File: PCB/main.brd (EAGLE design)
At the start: 98.1 x 68.5 mm, 81 parts, among them X1 BU-SMA-V

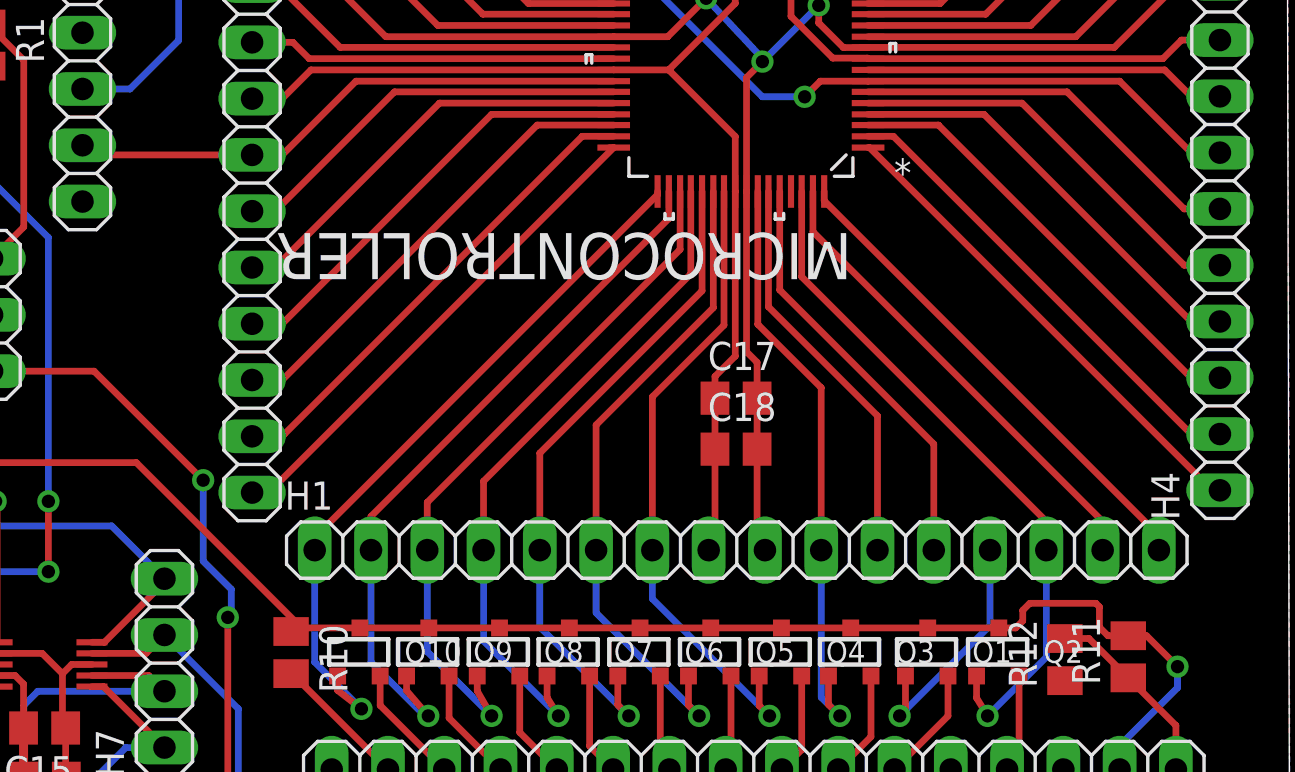
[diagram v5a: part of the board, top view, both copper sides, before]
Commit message: PCB Layout
-Tracks at bottom of pic made symmetrical
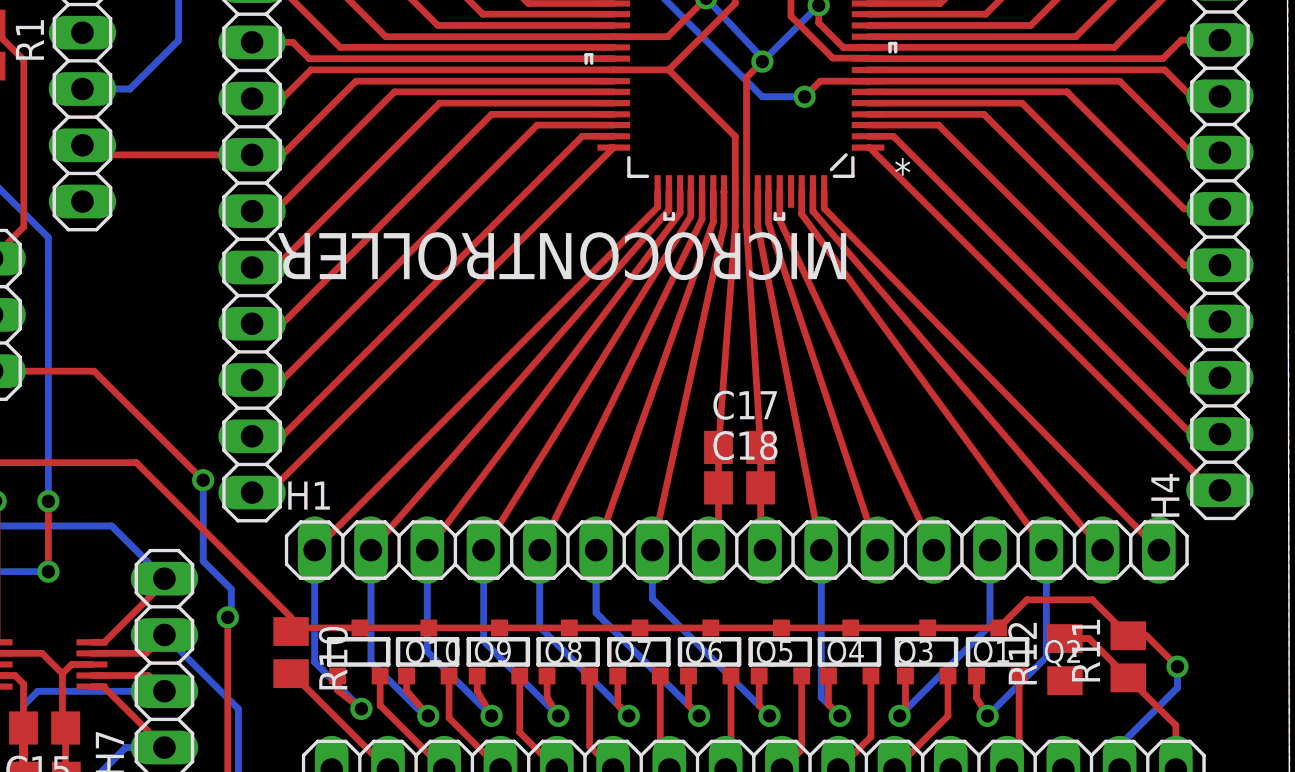
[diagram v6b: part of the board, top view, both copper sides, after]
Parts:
- moved C17 2.23 mm to (75.2, 23.9)
- moved C18 1.75 mm to (75.2, 22.0)
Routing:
- net PIC60: track 19.1 -> 17.7 mm
- net D3-PIC: track 30.4 -> 29.0 mm
- net D2-PIC: track 29.8 -> 28.5 mm
- net PIC59: track 18.2 -> 17.0 mm
- net D4-PIC: track 30.9 -> 29.7 mm
- net RS-PIC: track 31.3 -> 30.3 mm
- net D1-PIC: track 29.2 -> 28.2 mm
- net D5-PIC: track 31.6 -> 30.6 mm
- net D0-PIC: track 27.2 -> 26.3 mm
- net GND: track 162.0 -> 161.4 mm
- net PIC63: track 21.6 -> 21.0 mm
- net D6-PIC: track 32.6 -> 32.1 mm

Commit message: PCB + Schematic
- E-Pic issue fixed
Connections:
- net E-PIC: now also MICROCONTROLLER.61
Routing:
- net E-PIC: track 11.1 -> 29.8 mm
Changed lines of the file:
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@@
 <wire x1="82.39125" y1="11.7475" x2="86.4725" y2="15.82875" width="0.3048" layer="16"/>
 <wire x1="86.4725" y1="15.82875" x2="86.4725" y2="19.2275" width="0.3048" layer="16"/>
+<contactref element="MICROCONTROLLER" pad="61"/>
+<wire x1="77.4881" y1="35.4146" x2="77.4881" y2="34.3081" width="0.3048" layer="1"/>
+<wire x1="77.4881" y1="34.3081" x2="77.47" y2="34.29" width="0.3048" layer="1"/>
+<wire x1="77.47" y1="34.29" x2="86.4725" y2="19.2275" width="0.3048" layer="1"/>
 </signal>
 <signal name="RS-PIC">
